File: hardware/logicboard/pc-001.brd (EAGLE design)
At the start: 25 x 61.5 mm, 5 parts, among them J4 DNP, J5 DNP

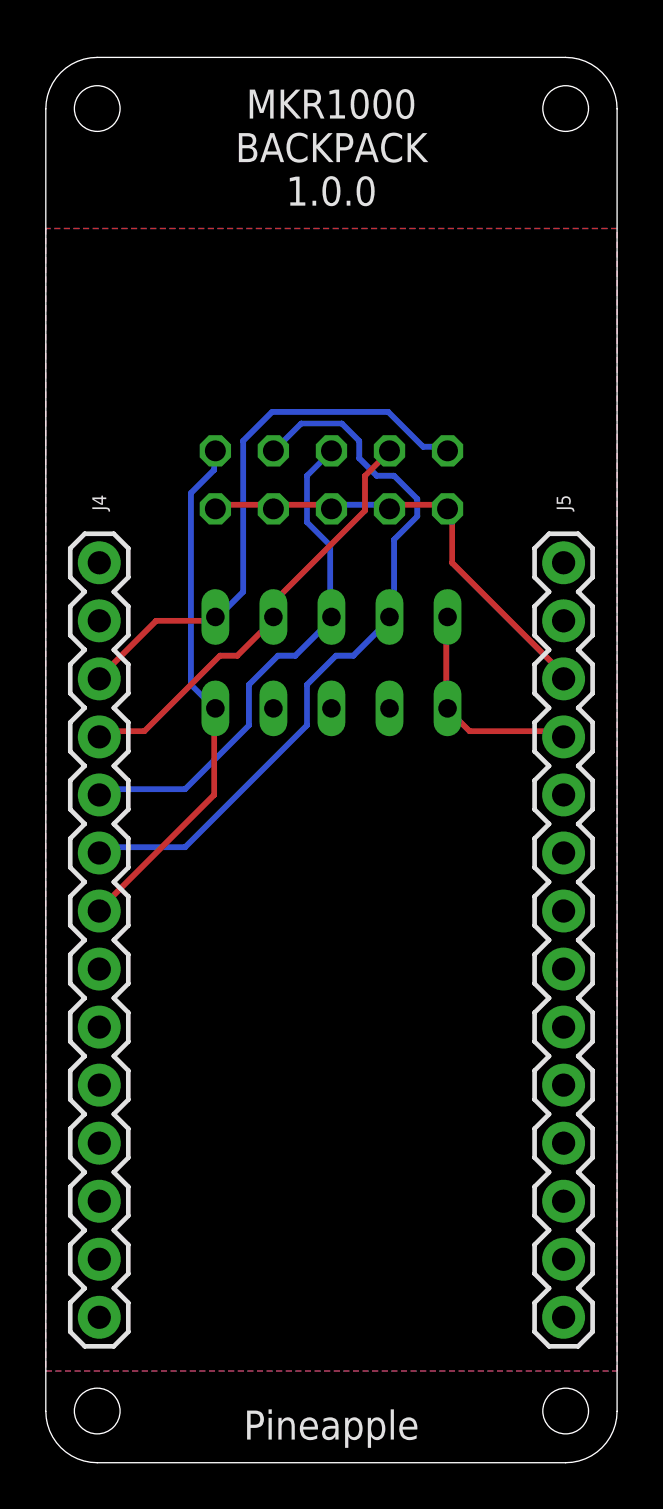
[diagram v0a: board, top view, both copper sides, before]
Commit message: New Pineapple Logo was put on the board.
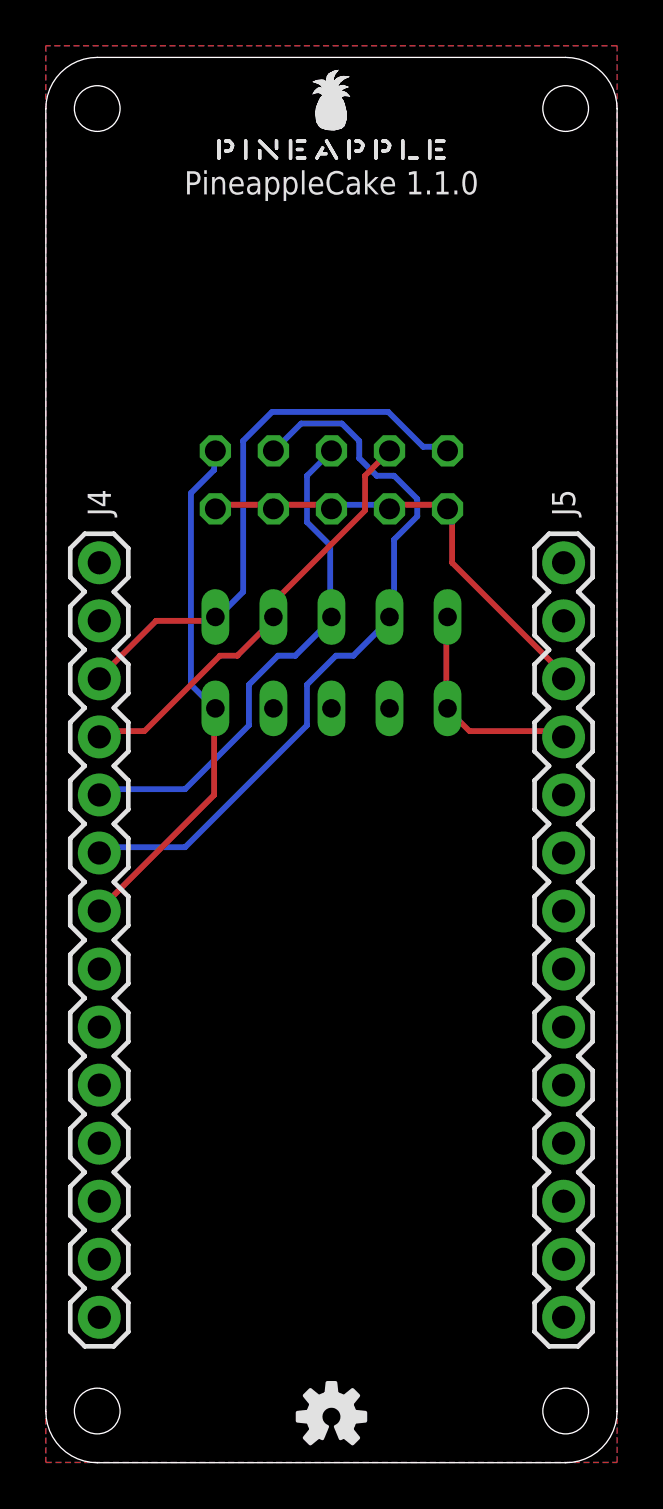
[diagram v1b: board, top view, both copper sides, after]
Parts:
- added LOGO1: OSHW-LOGOS, SparkFun-Aesthetics:OSHW-LOGO-S
- added U$1: PINEAPPLELOGO2SILKMINI, pineapplelogo:PINEAPPLELOGO2SILKMINI
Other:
- board text added: "PineappleCake 1.1.0"
- board text removed: "MKR1000 BACKPACK 1.0.0"
- board text removed: "Pineapple"
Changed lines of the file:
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@@
 <setting verticaltext="up"/>
 </settings>
-<grid distance="1" unitdist="mm" unit="mm" style="lines" multiple="1" display="yes" altdistance="0.01" altunitdist="mil" altunit="mm"/>
+<grid distance="1" unitdist="mm" unit="mm" style="dots" multiple="1" display="yes" altdistance="0.01" altunitdist="mil" altunit="mm"/>
 <layers>
 <layer number="1" name="Top" color="4" fill="1" visible="yes" active="yes"/>
@@
 <layer number="20" name="Dimension" color="15" fill="1" visible="yes" active="yes"/>
 <layer number="21" name="tPlace" color="7" fill="1" visible="yes" active="yes"/>
-<layer number="22" name="bPlace" color="7" fill="1" visible="yes" active="yes"/>
+<layer number="22" name="bPlace" color="7" fill="1" visible="no" active="yes"/>
 <layer number="23" name="tOrigins" color="15" fill="1" visible="yes" active="yes"/>
 <layer number="24" name="bOrigins" color="15" fill="1" visible="yes" active="yes"/>
@@
 <layer number="59" name="tCarbon" color="7" fill="1" visible="no" active="no"/>
 <layer number="60" name="bCarbon" color="7" fill="1" visible="no" active="no"/>
+<layer number="88" name="SimResults" color="9" fill="1" visible="no" active="no"/>
+<layer number="89" name="SimProbes" color="9" fill="1" visible="no" active="no"/>
 <layer number="90" name="Modules" color="5" fill="1" visible="no" active="no"/>
 <layer number="91" name="Nets" color="2" fill="1" visible="no" active="no"/>
@@
 <hole x="22.75" y="2.25" drill="2"/>
 <hole x="2.25" y="2.25" drill="2"/>
-<circle x="2.25" y="59.25" radius="1.97230625" width="0.254" layer="42"/>
-<circle x="22.75" y="59.25" radius="1.97230625" width="0.254" layer="42"/>
-<wire x1="2.3" y1="57.3" x2="0.05" y2="57.3" width="0.254" layer="42"/>
-<wire x1="4.2" y1="59.25" x2="4.2" y2="61.45" width="0.254" layer="42"/>
-<wire x1="20.8" y1="59.25" x2="20.8" y2="61.55" width="0.254" layer="42"/>
-<wire x1="22.7" y1="57.25" x2="24.95" y2="57.25" width="0.254" layer="42"/>
-<text x="12.5" y="55" size="1.27" layer="25" align="bottom-center">MKR1000
-BACKPACK
-1.0.0</text>
-<text x="12.5" y="1" size="1.27" layer="25" align="bottom-center">Pineapple</text>
+<text x="12.5" y="56" size="1.016" layer="25" align="center">PineappleCake 1.1.0</text>
 </plain>
 <attributes>
@@
 <elements>
 <element name="J5" library="SparkFun-Connectors" library_urn="urn:adsk.eagle:library:513" package="1X14" package3d_urn="urn:adsk.eagle:package:38183/1" value="DNP" x="22.66" y="6.3516" smashed="yes" rot="R90">
-<attribute name="NAME" x="22.66" y="42" size="0.6096" layer="25" font="vector" ratio="20" rot="R90" align="center"/>
+<attribute name="NAME" x="22.66" y="42" size="1.016" layer="25" font="vector" ratio="20" rot="R90" align="center"/>
 <attribute name="VALUE" x="24.692" y="5.0816" size="0.6096" layer="27" font="vector" ratio="20" rot="R90"/>
 </element>
 <element name="J4" library="SparkFun-Connectors" library_urn="urn:adsk.eagle:library:513" package="1X14" package3d_urn="urn:adsk.eagle:package:38183/1" value="DNP" x="2.34" y="39.3716" smashed="yes" rot="R270">
-<attribute name="NAME" x="2.34" y="42" size="0.6096" layer="25" font="vector" ratio="20" rot="R270" align="center"/>
+<attribute name="NAME" x="2.34" y="42" size="1.016" layer="25" font="vector" ratio="20" rot="R270" align="center"/>
 <attribute name="VALUE" x="0.308" y="40.6416" size="0.6096" layer="27" font="vector" ratio="20" rot="R270"/>
 </element>
@@
 <attribute name="MF" value="" x="12.5" y="37" size="1.778" layer="28" rot="MR0" display="off"/>
 <attribute name="MPN" value="" x="12.5" y="37" size="1.778" layer="28" rot="MR0" display="off"/>
-<attribute name="NAME" x="12.5" y="35" size="0.6096" layer="26" ratio="10" rot="MR0" align="center"/>
+<attribute name="NAME" x="12.5" y="35" size="1.016" layer="26" ratio="10" rot="MR0" align="center"/>
 <attribute name="OC_FARNELL" value="unknown" x="12.5" y="37" size="1.778" layer="28" rot="MR0" display="off"/>
 <attribute name="OC_NEWARK" value="unknown" x="12.5" y="37" size="1.778" layer="28" rot="MR0" display="off"/>
@@
 <attribute name="MF" value="" x="12.5" y="43" size="1.778" layer="28" rot="MR0" display="off"/>
 <attribute name="MPN" value="" x="12.5" y="43" size="1.778" layer="28" rot="MR0" display="off"/>
-<attribute name="NAME" x="12.5" y="40" size="0.8128" layer="26" ratio="10" rot="MR0" align="center"/>
+<attribute name="NAME" x="12.5" y="40" size="1.016" layer="26" ratio="10" rot="MR0" align="center"/>
 <attribute name="OC_FARNELL" value="unknown" x="12.5" y="43" size="1.778" layer="28" rot="MR0" display="off"/>
 <attribute name="OC_NEWARK" value="unknown" x="12.5" y="43" size="1.778" layer="28" rot="MR0" display="off"/>
@@
 <attribute name="MF" value="" x="12.5" y="33" size="1.778" layer="28" rot="MR0" display="off"/>
 <attribute name="MPN" value="" x="12.5" y="33" size="1.778" layer="28" rot="MR0" display="off"/>
-<attribute name="NAME" x="12.5" y="31" size="0.6096" layer="26" ratio="10" rot="MR0" align="center"/>
+<attribute name="NAME" x="12.5" y="31" size="1.016" layer="26" ratio="10" rot="MR0" align="center"/>
 <attribute name="OC_FARNELL" value="unknown" x="12.5" y="33" size="1.778" layer="28" rot="MR0" display="off"/>
 <attribute name="OC_NEWARK" value="unknown" x="12.5" y="33" size="1.778" layer="28" rot="MR0" display="off"/>
 <attribute name="VALUE" x="16.31" y="30.079" size="1.27" layer="28" ratio="10" rot="MR0"/>
 </element>
+<element name="LOGO1" library="SparkFun-Aesthetics" library_urn="urn:adsk.eagle:library:507" package="OSHW-LOGO-S" package3d_urn="urn:adsk.eagle:package:37099/1" value="OSHW-LOGOS" x="12.5" y="2"/>
+<element name="U$1" library="pineapplelogo" package="PINEAPPLELOGO2SILKMINI" value="PINEAPPLELOGO2SILKMINI" x="12.5" y="57"/>
 </elements>
 <signals>
@@
 <wire x1="22.606" y1="32.004" x2="22.66" y2="31.7516" width="0.254" layer="1"/>
 <wire x1="17.78" y1="32.766" x2="17.58" y2="33" width="0.254" layer="1"/>
-<polygon width="0.254" layer="1" thermals="no">
-<vertex x="0" y="4"/>
-<vertex x="25" y="4"/>
-<vertex x="25" y="54"/>
-<vertex x="0" y="54"/>
+<polygon width="0.127" layer="1">
+<vertex x="0" y="0"/>
+<vertex x="25" y="0"/>
+<vertex x="25" y="62"/>
+<vertex x="0" y="62"/>
 </polygon>
-<polygon width="0.254" layer="16" thermals="no">
-<vertex x="0" y="4"/>
-<vertex x="25" y="4"/>
-<vertex x="25" y="54"/>
-<vertex x="0" y="54"/>
+<polygon width="0.127" layer="16">
+<vertex x="0" y="0"/>
+<vertex x="25" y="0"/>
+<vertex x="25" y="62"/>
+<vertex x="0" y="62"/>
 </polygon>
 </signal>
@@
 </drawing>
 <compatibility>
-<note version="6.3" minversion="6.2.2" severity="warning">
-Since Version 6.2.2 text objects can contain more than one line,
-which will not be processed correctly with this version.
-</note>
 <note version="8.2" severity="warning">
 Since Version 8.2, EAGLE supports online libraries. The ids

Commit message: 14p Analog input.
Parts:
- ANALOG: device con-ml:ML10L -> con-ml:ML14L
- moved ANALOG 1.00 mm to (12.5, 44.0)
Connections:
- new net A0: ANALOG.2, J4.2, RN1.5
- new net A6: J4.8, RN2.3
- net A1: now also ANALOG.4, RN1.4; no longer ANALOG.2, RN1.5
- net A2: now also ANALOG.6, RN1.3; no longer ANALOG.4, RN1.4
- net A3: now also ANALOG.8, RN1.2; no longer ANALOG.6, RN1.3
- net A4: now also ANALOG.10, RN2.5; no longer ANALOG.8, RN1.2
- net A5: now also ANALOG.12, RN2.4; no longer ANALOG.10, RN2.5
- net VCC: now also ANALOG.11, ANALOG.13
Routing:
- net A4: track 32.4 -> 0.00 mm
- net A1: track 24.8 -> 0.00 mm
- net A5: track 23.1 -> 0.00 mm
- net A3: track 22.6 -> 0.00 mm
- net VCC: track 20.6 -> 0.00 mm
- net A2: track 19.3 -> 0.00 mm
- net GND: track 9.75 -> 0.00 mm

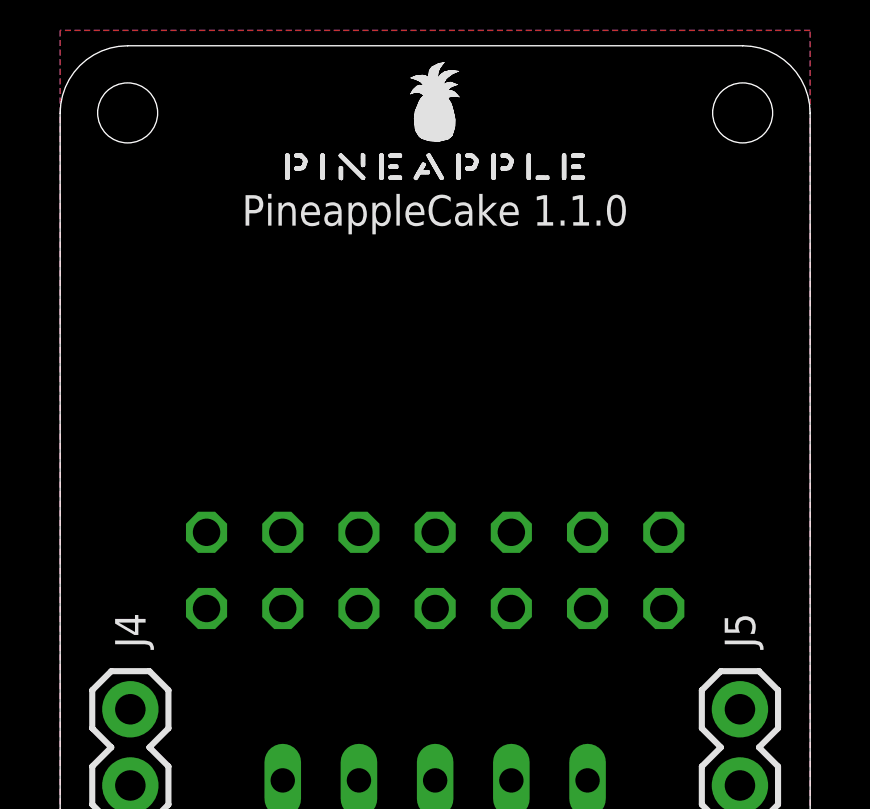
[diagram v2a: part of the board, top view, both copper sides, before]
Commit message: Layout of Analog input.
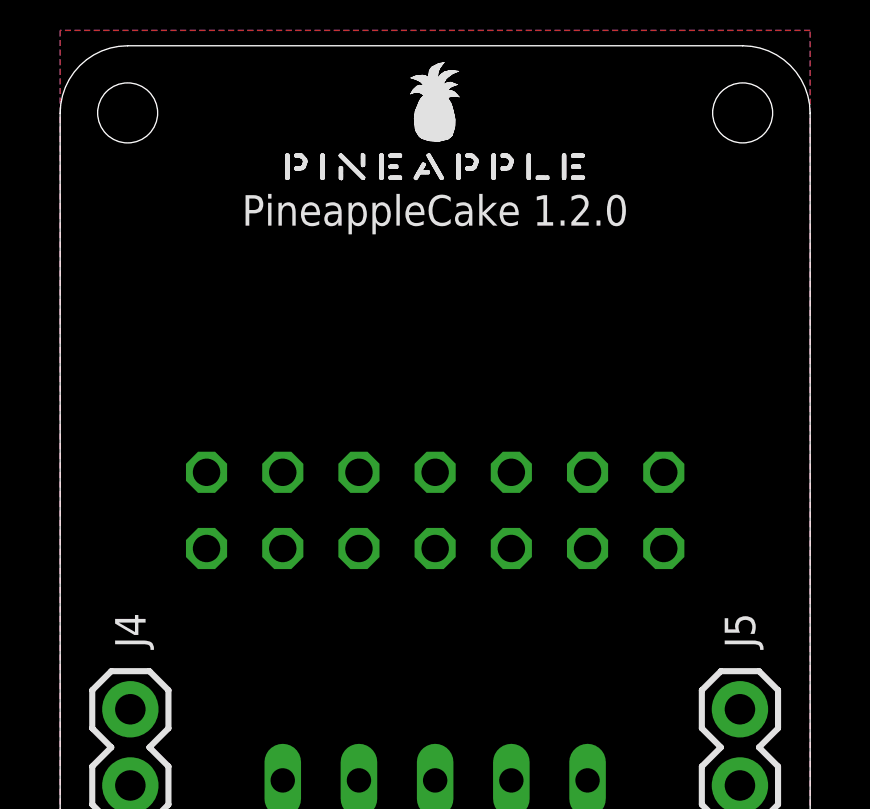
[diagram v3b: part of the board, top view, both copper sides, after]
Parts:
- moved ANALOG 2.00 mm to (12.5, 46.0)
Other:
- board text added: "PineappleCake 1.2.0"
- board text removed: "PineappleCake 1.1.0"
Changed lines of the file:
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@@
 <hole x="22.75" y="2.25" drill="2"/>
 <hole x="2.25" y="2.25" drill="2"/>
-<text x="12.5" y="56" size="1.016" layer="25" align="center">PineappleCake 1.1.0</text>
+<text x="12.5" y="56" size="1.016" layer="25" align="center">PineappleCake 1.2.0</text>
 </plain>
 <attributes>
@@
 <element name="LOGO1" library="SparkFun-Aesthetics" library_urn="urn:adsk.eagle:library:507" package="OSHW-LOGO-S" package3d_urn="urn:adsk.eagle:package:37099/1" value="OSHW-LOGOS" x="12.5" y="2"/>
 <element name="U$1" library="pineapplelogo" package="PINEAPPLELOGO2SILKMINI" value="PINEAPPLELOGO2SILKMINI" x="12.5" y="57"/>
-<element name="ANALOG" library="con-ml" library_urn="urn:adsk.eagle:library:164" package="ML14L" package3d_urn="urn:adsk.eagle:package:8677/1" value="" x="12.5" y="44" smashed="yes" rot="MR0">
-<attribute name="MF" value="" x="12.5" y="44" size="1.778" layer="28" rot="MR0" display="off"/>
-<attribute name="MPN" value="" x="12.5" y="44" size="1.778" layer="28" rot="MR0" display="off"/>
-<attribute name="NAME" x="12.5" y="40" size="1.016" layer="26" ratio="10" rot="MR0" align="center"/>
-<attribute name="OC_FARNELL" value="unknown" x="12.5" y="44" size="1.778" layer="28" rot="MR0" display="off"/>
-<attribute name="OC_NEWARK" value="unknown" x="12.5" y="44" size="1.778" layer="28" rot="MR0" display="off"/>
-<attribute name="VALUE" x="12.5254" y="55.43" size="1.778" layer="28" ratio="10" rot="MR0"/>
+<element name="ANALOG" library="con-ml" library_urn="urn:adsk.eagle:library:164" package="ML14L" package3d_urn="urn:adsk.eagle:package:8677/1" value="" x="12.5" y="46" smashed="yes" rot="MR0">
+<attribute name="MF" value="" x="12.5" y="46" size="1.778" layer="28" rot="MR0" display="off"/>
+<attribute name="MPN" value="" x="12.5" y="46" size="1.778" layer="28" rot="MR0" display="off"/>
+<attribute name="NAME" x="12.5" y="42" size="1.016" layer="26" ratio="10" rot="MR0" align="center"/>
+<attribute name="OC_FARNELL" value="unknown" x="12.5" y="46" size="1.778" layer="28" rot="MR0" display="off"/>
+<attribute name="OC_NEWARK" value="unknown" x="12.5" y="46" size="1.778" layer="28" rot="MR0" display="off"/>
+<attribute name="VALUE" x="12.5254" y="57.43" size="1.778" layer="28" ratio="10" rot="MR0"/>
 </element>
 </elements>
@@
 <contactref element="J4" pad="3"/>
 <wire x1="2.34" y1="34.2916" x2="9.96" y2="37" width="0" layer="19" extent="1-1"/>
-<wire x1="17.58" y1="45.27" x2="2.34" y2="34.2916" width="0" layer="19" extent="1-1"/>
+<wire x1="17.58" y1="47.27" x2="2.34" y2="34.2916" width="0" layer="19" extent="1-1"/>
 </signal>
 <signal name="A2">
@@
 <contactref element="J4" pad="4"/>
 <wire x1="2.34" y1="31.7516" x2="12.5" y2="37" width="0" layer="19" extent="1-1"/>
-<wire x1="15.04" y1="45.27" x2="2.34" y2="31.7516" width="0" layer="19" extent="1-1"/>
+<wire x1="15.04" y1="47.27" x2="2.34" y2="31.7516" width="0" layer="19" extent="1-1"/>
 </signal>
 <signal name="A3">
@@
 <contactref element="J4" pad="5"/>
 <wire x1="2.34" y1="29.2116" x2="15.04" y2="37" width="0" layer="19" extent="1-1"/>
-<wire x1="12.5" y1="45.27" x2="2.34" y2="29.2116" width="0" layer="19" extent="1-1"/>
+<wire x1="12.5" y1="47.27" x2="2.34" y2="29.2116" width="0" layer="19" extent="1-1"/>
 </signal>
 <signal name="A4">
@@
 <contactref element="J4" pad="6"/>
 <wire x1="2.34" y1="26.6716" x2="7.42" y2="33" width="0" layer="19" extent="1-1"/>
-<wire x1="9.96" y1="45.27" x2="2.34" y2="26.6716" width="0" layer="19" extent="1-1"/>
+<wire x1="9.96" y1="47.27" x2="2.34" y2="26.6716" width="0" layer="19" extent="1-1"/>
 </signal>
 <signal name="GND">
@@
 <contactref element="ANALOG" pad="13"/>
 <contactref element="ANALOG" pad="1"/>
-<wire x1="4.88" y1="42.73" x2="22.66" y2="34.2916" width="0" layer="19" extent="1-1"/>
-<wire x1="7.42" y1="42.73" x2="4.88" y2="42.73" width="0" layer="19" extent="1-1"/>
-<wire x1="9.96" y1="42.73" x2="7.42" y2="42.73" width="0" layer="19" extent="1-1"/>
-<wire x1="12.5" y1="42.73" x2="9.96" y2="42.73" width="0" layer="19" extent="1-1"/>
-<wire x1="15.04" y1="42.73" x2="12.5" y2="42.73" width="0" layer="19" extent="1-1"/>
-<wire x1="17.58" y1="42.73" x2="15.04" y2="42.73" width="0" layer="19" extent="1-1"/>
-<wire x1="20.12" y1="42.73" x2="17.58" y2="42.73" width="0" layer="19" extent="1-1"/>
+<wire x1="4.88" y1="44.73" x2="22.66" y2="34.2916" width="0" layer="19" extent="1-1"/>
+<wire x1="7.42" y1="44.73" x2="4.88" y2="44.73" width="0" layer="19" extent="1-1"/>
+<wire x1="9.96" y1="44.73" x2="7.42" y2="44.73" width="0" layer="19" extent="1-1"/>
+<wire x1="12.5" y1="44.73" x2="9.96" y2="44.73" width="0" layer="19" extent="1-1"/>
+<wire x1="15.04" y1="44.73" x2="12.5" y2="44.73" width="0" layer="19" extent="1-1"/>
+<wire x1="17.58" y1="44.73" x2="15.04" y2="44.73" width="0" layer="19" extent="1-1"/>
+<wire x1="20.12" y1="44.73" x2="17.58" y2="44.73" width="0" layer="19" extent="1-1"/>
 </signal>
 <signal name="A5">
@@
 <contactref element="J4" pad="7"/>
 <wire x1="2.34" y1="24.1316" x2="9.96" y2="33" width="0" layer="19" extent="1-1"/>
-<wire x1="7.42" y1="45.27" x2="2.34" y2="24.1316" width="0" layer="19" extent="1-1"/>
+<wire x1="7.42" y1="47.27" x2="2.34" y2="24.1316" width="0" layer="19" extent="1-1"/>
 </signal>
 <signal name="A0">
@@
 <contactref element="J4" pad="2"/>
 <wire x1="2.34" y1="36.8316" x2="7.42" y2="37" width="0" layer="19" extent="1-1"/>
-<wire x1="20.12" y1="45.27" x2="2.34" y2="36.8316" width="0" layer="19" extent="1-1"/>
+<wire x1="20.12" y1="47.27" x2="2.34" y2="36.8316" width="0" layer="19" extent="1-1"/>
 </signal>
 <signal name="A6">

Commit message: Routing.
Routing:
- net A3: track 0.00 -> 43.7 mm
- net A2: track 0.00 -> 39.1 mm
- net A0: track 0.00 -> 35.5 mm
- net A5: track 0.00 -> 32.5 mm
- net A1: track 0.00 -> 28.6 mm
- net VCC: track 0.00 -> 26.9 mm
- net A4: track 0.00 -> 23.8 mm
- net A6: track 0.00 -> 15.6 mm
- net GND: track 0.00 -> 9.75 mm
